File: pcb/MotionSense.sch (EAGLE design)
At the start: 18 parts

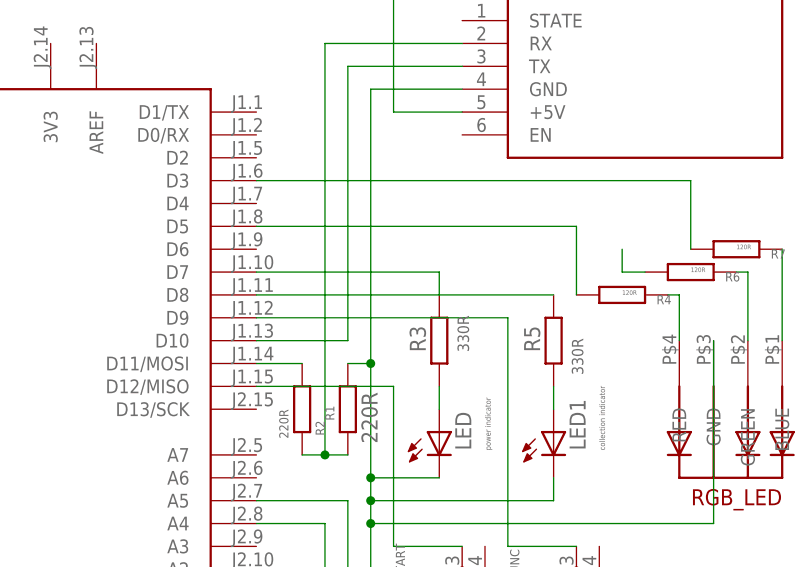
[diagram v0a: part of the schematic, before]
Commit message: [UPDATE] power and collection led connection inverted correction
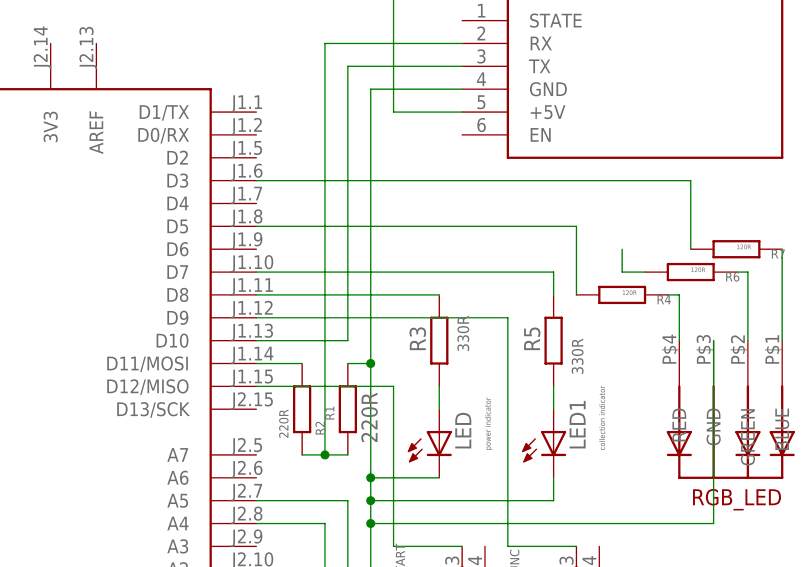
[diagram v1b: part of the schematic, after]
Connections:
- net N$13: now also R3.2; no longer R5.2
- net N$9: now also R5.2; no longer R3.2
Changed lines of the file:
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@@
-</segment>
-</net>
-<net name="N$9" class="0">
-<segment>
-<pinref part="R3" gate="G$1" pin="2"/>
-<wire x1="96.52" y1="76.2" x2="96.52" y2="78.74" width="0.1524" layer="91"/>
-<wire x1="96.52" y1="78.74" x2="76.2" y2="78.74" width="0.1524" layer="91"/>
-<pinref part="ARDUINO-NANO" gate="MODUL" pin="D7"/>
 </segment>
 </net>
@@
 </segment>
 </net>
-<net name="N$13" class="0">
-<segment>
-<pinref part="R5" gate="G$1" pin="2"/>
-<pinref part="ARDUINO-NANO" gate="MODUL" pin="D8"/>
-<wire x1="109.22" y1="76.2" x2="76.2" y2="76.2" width="0.1524" layer="91"/>
-</segment>
-</net>
 <net name="N$21" class="0">
 <segment>
@@
 </segment>
 </net>
+<net name="N$9" class="0">
+<segment>
+<pinref part="ARDUINO-NANO" gate="MODUL" pin="D7"/>
+<pinref part="R5" gate="G$1" pin="2"/>
+<wire x1="76.2" y1="78.74" x2="109.22" y2="78.74" width="0.1524" layer="91"/>
+<wire x1="109.22" y1="78.74" x2="109.22" y2="76.2" width="0.1524" layer="91"/>
+</segment>
+</net>
+<net name="N$13" class="0">
+<segment>
+<pinref part="ARDUINO-NANO" gate="MODUL" pin="D8"/>
+<pinref part="R3" gate="G$1" pin="2"/>
+<wire x1="76.2" y1="76.2" x2="96.52" y2="76.2" width="0.1524" layer="91"/>
+</segment>
+</net>
